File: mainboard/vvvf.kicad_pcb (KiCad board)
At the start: 4 copper layers, 100 x 100 mm, 81 parts, among them J1 Conn_01x16_Pin, J2 Screw_Terminal_01x01, J3 Screw_Terminal_01x01, J4 Screw_Terminal_01x01, J5 Screw_Terminal_01x01, J6 Screw_Terminal_01x02, J7 Screw_Terminal_01x01, J8 Screw_Terminal_01x01, J9 Screw_Terminal_01x02, U11 LM7805_TO220, U12 AMC1303M2510DWVR, U3 UCC21520ADW, U4 TLP152, U5 ACS758KCB-150B-PFF-T, U6 UCC21520ADW, U7 UCC21520ADW, U8 ACS758KCB-150B-PFF-T, U9 ACS758KCB-150B-PFF-T

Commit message: current sense board
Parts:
- added J10: Conn_01x05_Pin, Connector_PinHeader_2.54mm:PinHeader_1x05_P2.54mm_Vertical, F.Cu at (95.2, 63.3)
- J1: value Conn_01x16_Pin -> Connector to external IGBT Module
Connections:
- R30 pad 2: /ADC0 -> /ADC2
- R31 pad 1: /ADC0 -> /ADC2
- U4 pad 1: GPXX -> /GP12
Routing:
- net GND: track 22.9 -> 24.2 mm, vias 4 -> 5
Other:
- board size 100 x 100 mm -> 100 x 76.6 mm
- board text added: "1"
- board text added: "10"
- board text added: "11"
- board text added: "12"
- board text added: "13"
- board text added: "14"
- board text added: "15"
- board text added: "16"
- board text added: "2"
- board text added: "3"
- board text added: "4"
- board text added: "5"
- board text added: "5V"
- board text added: "6"
- board text added: "7"
- board text added: "8"
- board text added: "9"
- board text added: "CS0"
- board text added: "CS1"
- board text added: "CS2"
- board text added: "GND"

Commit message: did stuff
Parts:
- removed C10, C37, C38: 100nF, Capacitor_SMD:C_0603_1608Metric_Pad1.08x0.95mm_HandSolder
- removed J2, J3, J4, J5, J7, J8: Screw_Terminal_01x01, easyeda2kicad:CONN-TH_T44001
- removed R13, R28, R30: 10k, Resistor_SMD:R_0603_1608Metric_Pad0.98x0.95mm_HandSolder
- removed R14, R29, R31: 6.8k, Resistor_SMD:R_0603_1608Metric_Pad0.98x0.95mm_HandSolder
- removed U5, U8, U9: ACS758KCB-150B-PFF-T, easyeda2kicad:SENSOR-TH_ACS758KCB-150B-PFF-T
- added C23: 22uF, Capacitor_SMD:C_0805_2012Metric_Pad1.18x1.45mm_HandSolder, F.Cu at (110.9, 96.5)
- added C24: 22uF, Capacitor_SMD:C_0805_2012Metric_Pad1.18x1.45mm_HandSolder, F.Cu at (114.9, 96.5)
- added C25: 100nF, Capacitor_SMD:C_0603_1608Metric_Pad1.08x0.95mm_HandSolder, F.Cu at (118.2, 79.5)
- added C35: 10uF, Capacitor_SMD:C_0603_1608Metric_Pad1.08x0.95mm_HandSolder, F.Cu at (104.6, 91.4)
- added C36: 470pF, easyeda2kicad:CAP-TH_L5.5-W3.2-P5.00-D0.5, F.Cu at (102.8, 85.6)
- added SW1: SW_Push, easyeda2kicad:SW-SMD_4P-L4.2-W3.3-P2.15-LS5.1, F.Cu at (153.8, 77.7)
- moved C17 35.6 mm to (182.4, 78.0)
- moved U11 2.37 mm to (109.7, 93.8)
- moved R22 1.08 mm to (145.4, 77.6), turned to 0 degrees
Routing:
- net /ADC2: track 0.00 -> 86.8 mm
- net /ADC1: track 0.00 -> 80.7 mm
- net /ADC0: track 0.00 -> 79.0 mm
- net /GP12: track 0.00 -> 46.0 mm
- net /GP2: track 0.00 -> 33.1 mm
- net +5V: track 155.0 -> 187.4 mm, vias 1 -> 5
- net /GP0: track 0.00 -> 31.7 mm
- net +12V: track 141.5 -> 153.7 mm
- net Net-(A1-RUN): track 0.00 -> 11.1 mm
- net GND: track 24.2 -> 34.6 mm, vias 5 -> 9
- net GNDPWR: track 37.5 -> 44.5 mm, vias 4 -> 5
- net (no net): track 4.56 -> 0.00 mm
- net +5V_UNISOLATED: track 6.38 -> 9.39 mm
- net +3V3: track 0.00 -> 1.79 mm
- net /GP15: track 2.27 -> 3.71 mm
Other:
- board text added: "NC"

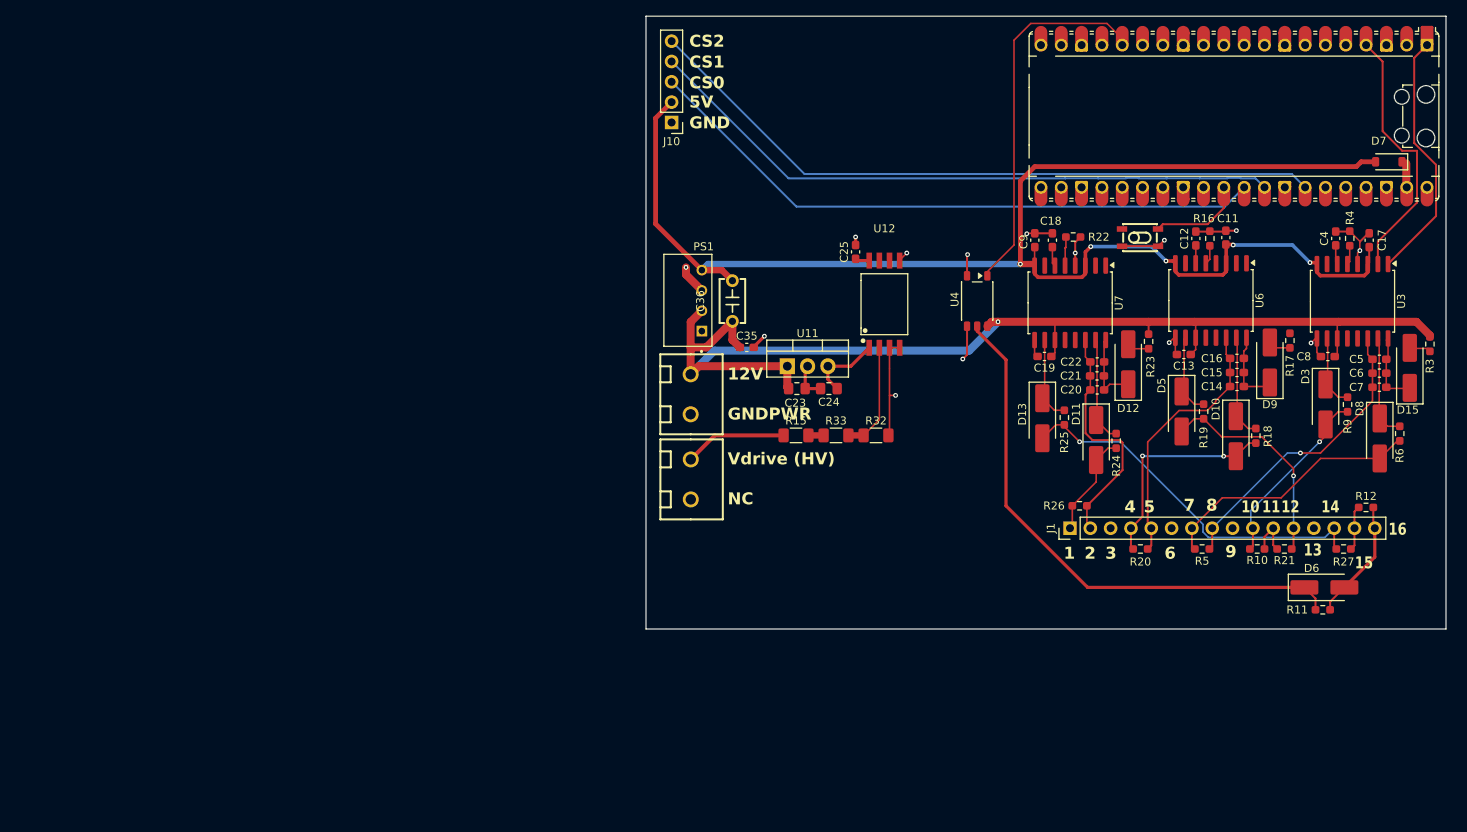
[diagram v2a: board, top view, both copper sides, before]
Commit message: New isolated ADC, add decoupling capacitors
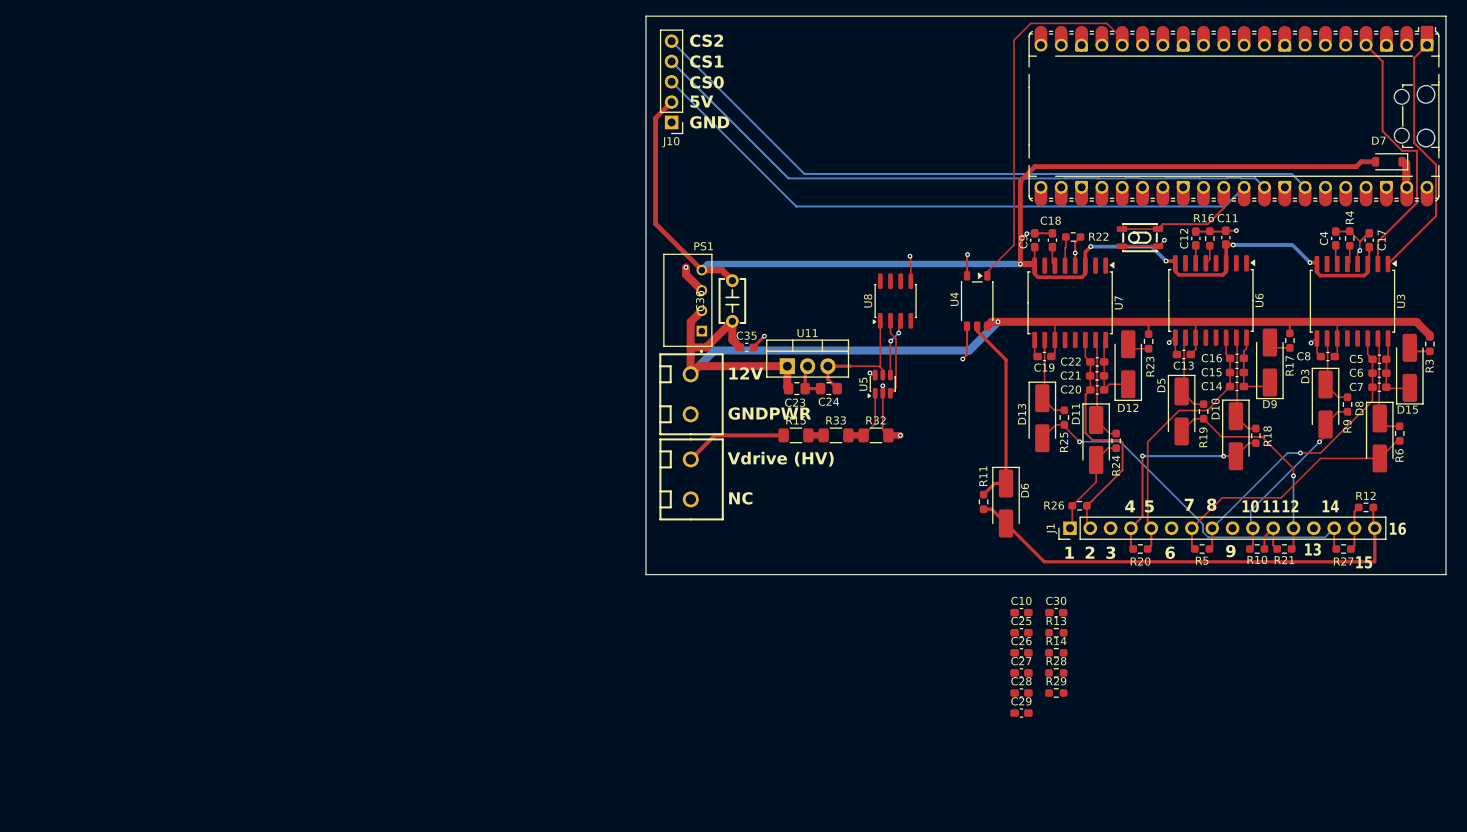
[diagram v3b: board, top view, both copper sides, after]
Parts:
- removed U12: AMC1303M2510DWVR, easyeda2kicad:SOIC-8_L7.5-W5.9-P1.27-LS11.5-BL-1
- added C10: 100nF, Capacitor_SMD:C_0603_1608Metric_Pad1.08x0.95mm_HandSolder, F.Cu at (138.9, 124.6)
- added C26: 10uF, Capacitor_SMD:C_0603_1608Metric_Pad1.08x0.95mm_HandSolder, F.Cu at (138.9, 129.6)
- added C27: 1uF, Capacitor_SMD:C_0603_1608Metric_Pad1.08x0.95mm_HandSolder, F.Cu at (138.9, 132.1)
- added C28: 100nF, Capacitor_SMD:C_0603_1608Metric_Pad1.08x0.95mm_HandSolder, F.Cu at (138.9, 134.6)
- added C29: 100nF, Capacitor_SMD:C_0603_1608Metric_Pad1.08x0.95mm_HandSolder, F.Cu at (138.9, 137.1)
- added C30: 100nF, Capacitor_SMD:C_0603_1608Metric_Pad1.08x0.95mm_HandSolder, F.Cu at (143.3, 124.6)
- added R13: 22k, Resistor_SMD:R_0603_1608Metric_Pad0.98x0.95mm_HandSolder, F.Cu at (143.3, 127.1)
- added R14: 22k, Resistor_SMD:R_0603_1608Metric_Pad0.98x0.95mm_HandSolder, F.Cu at (143.3, 129.6)
- added R28: 22k, Resistor_SMD:R_0603_1608Metric_Pad0.98x0.95mm_HandSolder, F.Cu at (143.3, 132.1)
- added R29: 22k, Resistor_SMD:R_0603_1608Metric_Pad0.98x0.95mm_HandSolder, F.Cu at (143.3, 134.6)
- added U5: MCP3421A0T-ECH, Package_TO_SOT_SMD:SOT-23-6, F.Cu at (121.6, 96.0)
- added U8: ISO1540, Package_SO:SOIC-8_3.9x4.9mm_P1.27mm, F.Cu at (123.2, 85.6)
- C25: value 100nF -> 10uF
- R32: value 1k -> 10k
- moved C25 51.9 mm to (138.9, 127.1), turned to 0 degrees
- moved R11 44.5 mm to (134.2, 110.7), turned to -90 degrees
- moved D6 41.2 mm to (137.0, 110.9), turned to -90 degrees
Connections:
- C25 pad 1: +3V3 -> +5V_UNISOLATED
- C25 pad 2: GND -> GNDPWR
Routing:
- net Net-(D6-K): track 68.8 -> 24.5 mm
- net /IGBT_BRAKE_G: track 15.2 -> 58.5 mm
- net Net-(U5-SCL): track 0.00 -> 9.64 mm
- net +5V_UNISOLATED: track 9.39 -> 16.8 mm
- net Net-(U5-SDA): track 0.00 -> 7.32 mm, vias 0 -> 2
- net Net-(U5-Vin+): track 13.7 -> 7.76 mm
- net Net-(A1-RUN): track 11.1 -> 15.6 mm
- net GNDPWR: track 44.5 -> 40.4 mm, vias 5 -> 7
- net +3V3: track 1.79 -> 0.00 mm
- net +12V: track 153.7 -> 155.2 mm
- net GND: track 34.6 -> 35.5 mm, vias 9 -> 8
- net Net-(D15-A): track 2.69 -> 3.31 mm
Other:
- board size 100 x 76.6 mm -> 100 x 69.8 mm

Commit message: Almost done routing
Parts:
- removed C28: 100nF, Capacitor_SMD:C_0603_1608Metric_Pad1.08x0.95mm_HandSolder
- removed C36: 470pF, easyeda2kicad:CAP-TH_L5.5-W3.2-P5.00-D0.5
- removed R15: 1M, Resistor_SMD:R_1206_3216Metric_Pad1.30x1.75mm_HandSolder
- C27: value 1uF -> 10uF
- R13, R14, R28, R29: value 22k -> 10k
- R33: value 1M -> 2M
- moved C27 63.9 mm to (102.5, 79.6), turned to 180 degrees
- moved R14 55.1 mm to (124.5, 77.8), turned to -90 degrees
- moved R13 53.3 mm to (123.0, 77.8), turned to -90 degrees
- moved C30 51.6 mm to (121.4, 77.8), turned to 90 degrees
- moved R29 48.0 mm to (121.6, 91.8)
- moved C29 46.3 mm to (125.2, 92.9), turned to 90 degrees
- moved R28 40.4 mm to (125.2, 95.9), turned to 180 degrees
- moved C26 39.4 mm to (137.3, 90.2), turned to 180 degrees
- moved C25 31.8 mm to (124.0, 99.0), turned to 180 degrees
- moved C10 28.2 mm to (124.0, 100.6), turned to 180 degrees
- moved C7 3.50 mm to (183.7, 92.9)
- moved C5 3.32 mm to (183.7, 96.2)
- moved C35 0.80 mm to (104.6, 92.2)
- moved R32 0.60 mm to (120.8, 103.0)
- moved R33 0.60 mm to (115.8, 103.0)
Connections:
- C27 pad 1: +12V -> +5V
- C27 pad 2: Net-(D6-K) -> GND
- C30 pad 2: GNDPWR -> GND
- R28 pad 1: +3V3 -> +5V_UNISOLATED
- R29 pad 1: +3V3 -> +5V_UNISOLATED
- R33 pad 1: Net-(R15-Pad2) -> Vdrive
- U8 pad 2: Net-(U5-SCL) -> Net-(U5-SDA)
- U8 pad 3: Net-(U5-SDA) -> Net-(U5-SCL)
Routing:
- net /GP19: track 0.00 -> 34.8 mm, vias 0 -> 1
- net /GP18: track 0.00 -> 33.6 mm, vias 0 -> 1
- net +5V_UNISOLATED: track 16.8 -> 34.5 mm, vias 0 -> 1
- net +3V3: track 0.00 -> 8.47 mm
- net GNDPWR: track 40.4 -> 48.5 mm, vias 7 -> 9
- net Vdrive: track 12.8 -> 17.6 mm
- net +12V: track 155.2 -> 150.7 mm
- net Net-(D6-K): track 24.5 -> 26.6 mm
- net GND: track 35.5 -> 37.4 mm, vias 8 -> 10
- net Net-(R15-Pad2): track 1.90 -> 0.00 mm
- net Net-(U5-SCL): track 9.64 -> 11.1 mm
- net +5V: track 187.4 -> 188.0 mm
- net Net-(U5-Vin+): track 7.76 -> 8.36 mm
- net Net-(U5-SDA): track 7.32 -> 6.79 mm, vias 2 -> 0

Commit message: order for mainboard v1.0
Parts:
- added C28: 33pF, Capacitor_SMD:C_0603_1608Metric_Pad1.08x0.95mm_HandSolder, F.Cu at (189.2, 78.4)
- added C31: 33pF, Capacitor_SMD:C_0603_1608Metric_Pad1.08x0.95mm_HandSolder, F.Cu at (188.0, 79.6)
- added C32: 33pF, Capacitor_SMD:C_0603_1608Metric_Pad1.08x0.95mm_HandSolder, F.Cu at (171.2, 78.6)
- added C33: 33pF, Capacitor_SMD:C_0603_1608Metric_Pad1.08x0.95mm_HandSolder, F.Cu at (171.2, 80.2)
- added C34: 33pF, Capacitor_SMD:C_0603_1608Metric_Pad1.08x0.95mm_HandSolder, F.Cu at (154.2, 79.6)
- added C36: 33pF, Capacitor_SMD:C_0603_1608Metric_Pad1.08x0.95mm_HandSolder, F.Cu at (153.0, 81.2)
- added R15: 3k, Capacitor_SMD:C_0603_1608Metric_Pad1.08x0.95mm_HandSolder, F.Cu at (159.2, 77.8)
- added R30: 3k, Capacitor_SMD:C_0603_1608Metric_Pad1.08x0.95mm_HandSolder, F.Cu at (176.4, 77.7)
- added R31: 3k, Capacitor_SMD:C_0603_1608Metric_Pad1.08x0.95mm_HandSolder, F.Cu at (141.5, 77.9)
- added R34: 51R, Resistor_SMD:R_0603_1608Metric_Pad0.98x0.95mm_HandSolder, F.Cu at (186.8, 77.0)
- added R35: 51R, Resistor_SMD:R_0603_1608Metric_Pad0.98x0.95mm_HandSolder, F.Cu at (185.6, 76.0)
- added R36: 51R, Resistor_SMD:R_0603_1608Metric_Pad0.98x0.95mm_HandSolder, F.Cu at (168.6, 78.4)
- added R37: 51R, Resistor_SMD:R_0603_1608Metric_Pad0.98x0.95mm_HandSolder, F.Cu at (166.6, 77.6)
- added R38: 51R, Resistor_SMD:R_0603_1608Metric_Pad0.98x0.95mm_HandSolder, F.Cu at (151.4, 78.8)
- added R39: 51R, Resistor_SMD:R_0603_1608Metric_Pad0.98x0.95mm_HandSolder, F.Cu at (150.0, 78.0)
- D10, D11, D13, D3, D5, D8: value ES1D -> SS34; footprint Diode_SMD:D_SMA_Handsoldering -> Diode_SMD:D_SMA
- D12, D15, D6, D9: value ES1D -> STTH1R06; footprint Diode_SMD:D_SMA_Handsoldering -> Diode_THT:D_DO-41_SOD81_P7.62mm_Horizontal
- R17, R23, R3: footprint Resistor_SMD:R_0603_1608Metric_Pad0.98x0.95mm_HandSolder -> Resistor_SMD:R_1210_3225Metric_Pad1.30x2.65mm_HandSolder
- moved SW1 22.5 mm to (135.6, 64.4), turned to 90 degrees
- moved R26 4.94 mm to (142.0, 113.8), turned to -90 degrees
- moved D9 4.72 mm to (170.0, 98.0)
- moved D12 4.70 mm to (152.3, 98.2)
- moved D15 4.66 mm to (187.2, 98.6)
- moved D6 4.53 mm to (137.2, 106.4)
- moved R12 3.85 mm to (182.6, 115.2)
- moved C8 2.23 mm to (179.2, 93.6), turned to -90 degrees
- moved C13 1.65 mm to (160.6, 93.2), turned to -90 degrees
- moved C19 1.61 mm to (143.2, 93.3), turned to -90 degrees
- moved J1 1.40 mm to (145.0, 112.6)
- moved R10 1.40 mm to (168.4, 115.2)
- moved R20 1.40 mm to (153.8, 115.2)
- moved R21 1.40 mm to (171.8, 115.2)
- moved R27 1.40 mm to (179.2, 115.2)
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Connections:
- U3 pad 1: /GP0 -> Net-(U3-INA)
- U3 pad 2: /GP2 -> Net-(U3-INB)
- U6 pad 1: /GP4 -> Net-(U6-INA)
- U6 pad 2: /GP6 -> Net-(U6-INB)
- U7 pad 1: /GP8 -> Net-(U7-INA)
- U7 pad 2: /GP10 -> Net-(U7-INB)
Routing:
- net +3V3: track 8.47 -> 65.5 mm, vias 0 -> 1
- net /GP13: track 2.41 -> 56.8 mm, vias 0 -> 2
- net /GP14: track 2.39 -> 43.3 mm, vias 0 -> 1
- net /GP8: track 0.00 -> 32.7 mm, vias 0 -> 1
- net /GP10: track 0.00 -> 28.9 mm, vias 0 -> 1
- net /GP4: track 0.00 -> 27.9 mm, vias 0 -> 1
- net GND: track 37.4 -> 65.2 mm, vias 10 -> 15
- net /GP15: track 3.71 -> 30.8 mm, vias 0 -> 1
- net /GP6: track 0.00 -> 24.2 mm, vias 0 -> 1
- net Net-(A1-RUN): track 15.6 -> 36.1 mm, vias 0 -> 2
- net Net-(U3-INB): track 0.00 -> 9.05 mm
- net Net-(U7-INB): track 0.00 -> 7.34 mm
- net Net-(U3-INA): track 0.00 -> 7.16 mm
- net /GP2: track 33.1 -> 26.3 mm
- net /GP21: track 0.00 -> 6.03 mm
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- added copper zone on In1.Cu, net GND
- added copper zone on In1.Cu, net GNDPWR
- removed copper zone on In2.Cu, net GND
- removed copper zone on In2.Cu, net GNDPWR
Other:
- board size 100 x 69.8 mm -> 100 x 68.4 mm
- board text added: "Revision 1 Designed by Alex Park"
- board text added: "VVVF Inverter"

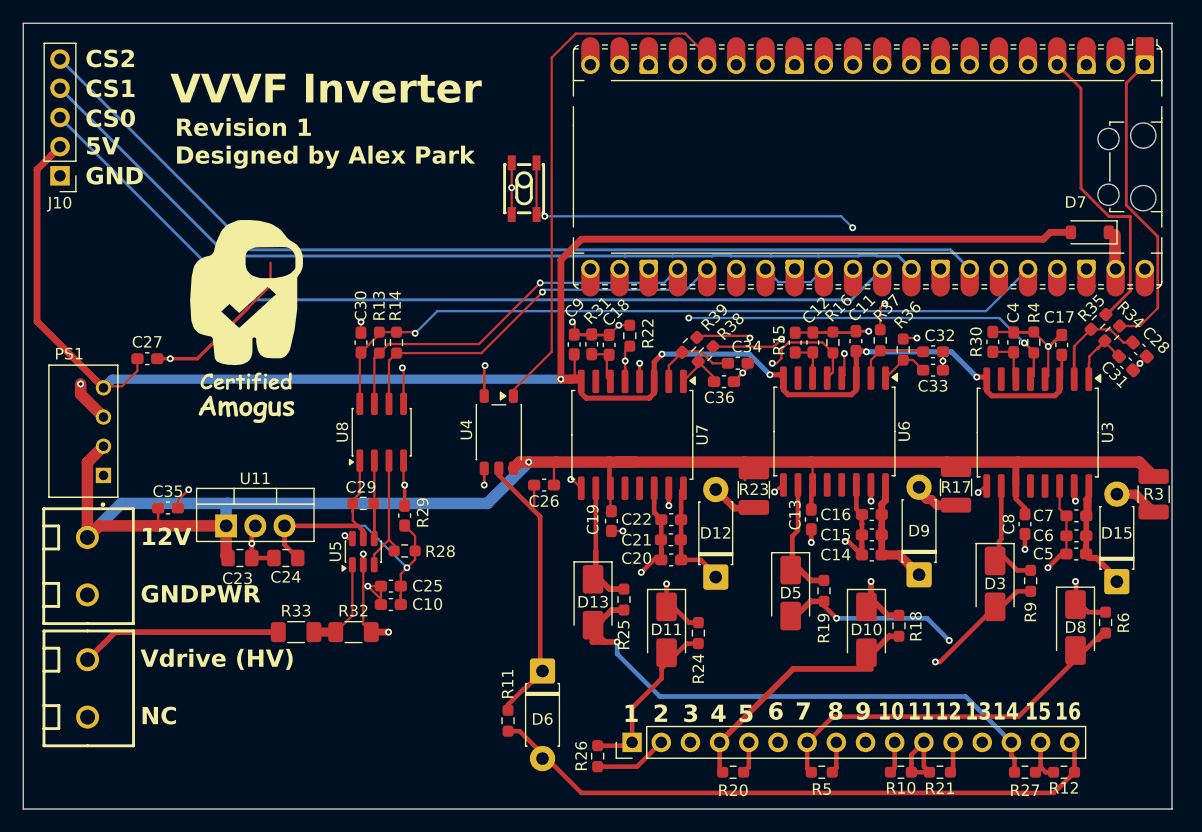
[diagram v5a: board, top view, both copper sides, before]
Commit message: mounting holes
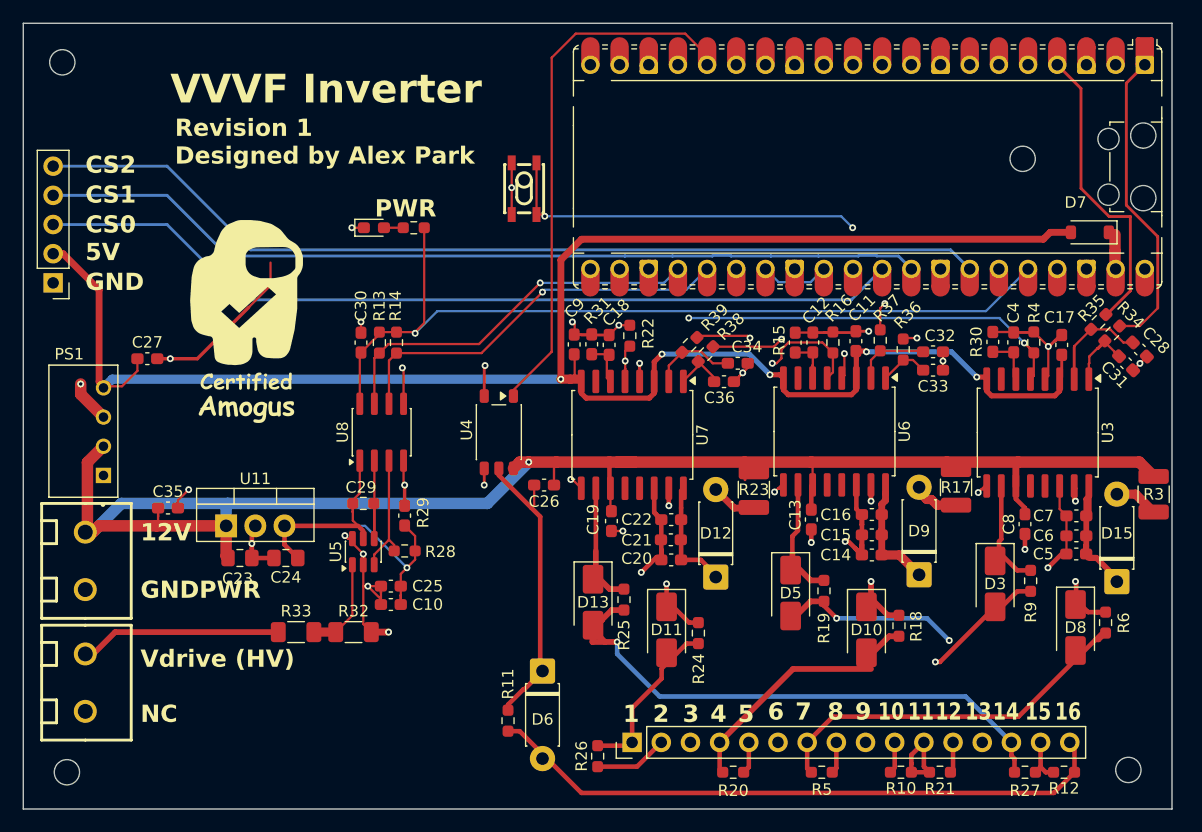
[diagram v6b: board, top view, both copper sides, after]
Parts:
- added D14: GREEN, LED_SMD:LED_0603_1608Metric_Pad1.05x0.95mm_HandSolder, F.Cu at (122.5, 67.8)
- added H1: MountingHole, MountingHole:MountingHole_2.2mm_M2, F.Cu at (95.4, 53.4)
- added H2: MountingHole, MountingHole:MountingHole_2.2mm_M2, F.Cu at (179.0, 61.8)
- added H3: MountingHole, MountingHole:MountingHole_2.2mm_M2, F.Cu at (188.2, 115.0)
- added H4: MountingHole, MountingHole:MountingHole_2.2mm_M2, F.Cu at (95.8, 115.2)
- added R40: 220, Resistor_SMD:R_0603_1608Metric_Pad0.98x0.95mm_HandSolder, F.Cu at (126.0, 67.8)
- moved J10 9.34 mm to (94.6, 72.6)
- moved J9 0.54 mm to (97.4, 107.4)
- moved J6 0.50 mm to (97.4, 96.8)
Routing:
- net +5V: track 185.4 -> 174.9 mm
- net +3V3: track 65.5 -> 75.0 mm
- net /ADC0: track 79.3 -> 76.0 mm
- net /ADC1: track 80.7 -> 77.5 mm
- net /ADC2: track 86.8 -> 83.5 mm
- net GNDPWR: track 45.2 -> 47.0 mm
- net Net-(D14-A): track 0.00 -> 1.68 mm
- net GND: track 65.2 -> 66.2 mm, vias 15 -> 16
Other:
- board text added: "PWR"
